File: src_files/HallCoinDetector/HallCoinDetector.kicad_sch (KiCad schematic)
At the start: 30 parts, among them M1 Motor_DC 3V, Q2 BSS214NW, U1 SE555D, U2 TPS61070, U3 49E Hall, U4 LM393

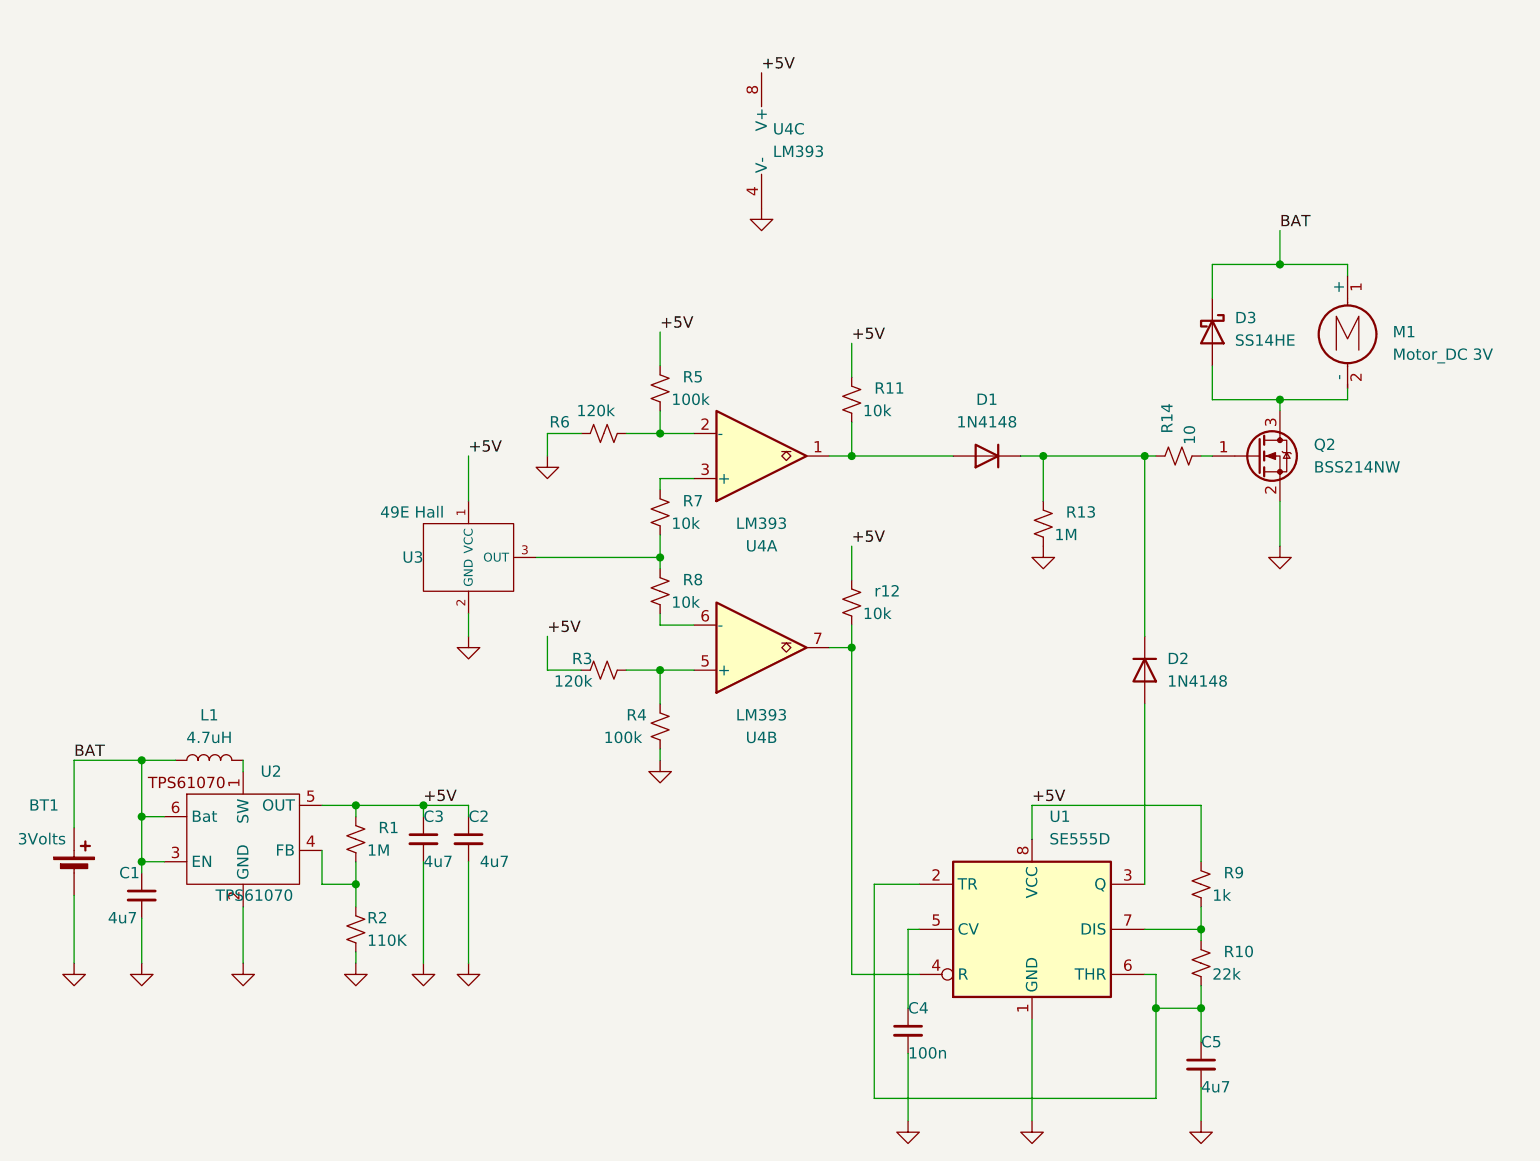
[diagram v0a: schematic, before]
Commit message: diseño de librerias y ubicación de componentes
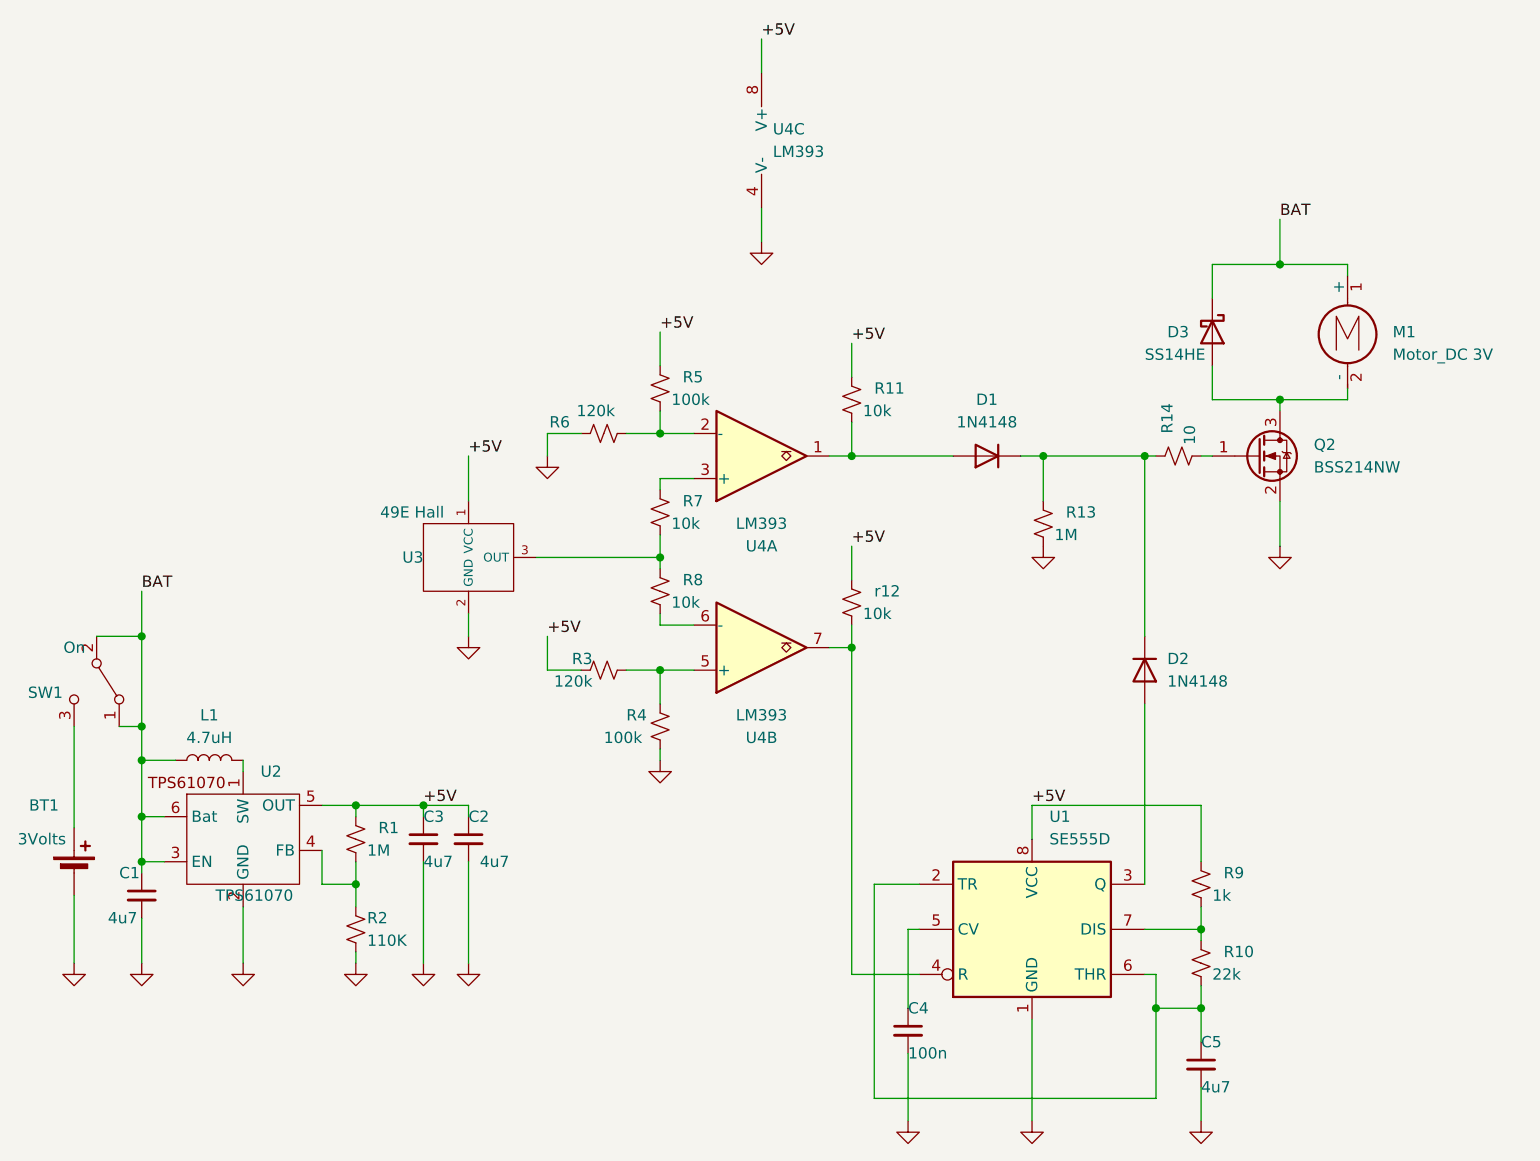
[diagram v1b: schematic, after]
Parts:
- added SW1: On, Button_Switch_SMD:SW_SPDT_PCM12, symbol Switch:SW_SPDT
- BT1: footprint BatteryHolder_Keystone_3002_1x2032 -> Batery Holder:cr1616
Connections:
- net BAT: now also SW1.1 (A), SW1.2 (B); no longer BT1.1 (+)
- new net: BT1.1 (+), SW1.3 (C)

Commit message: delete backups
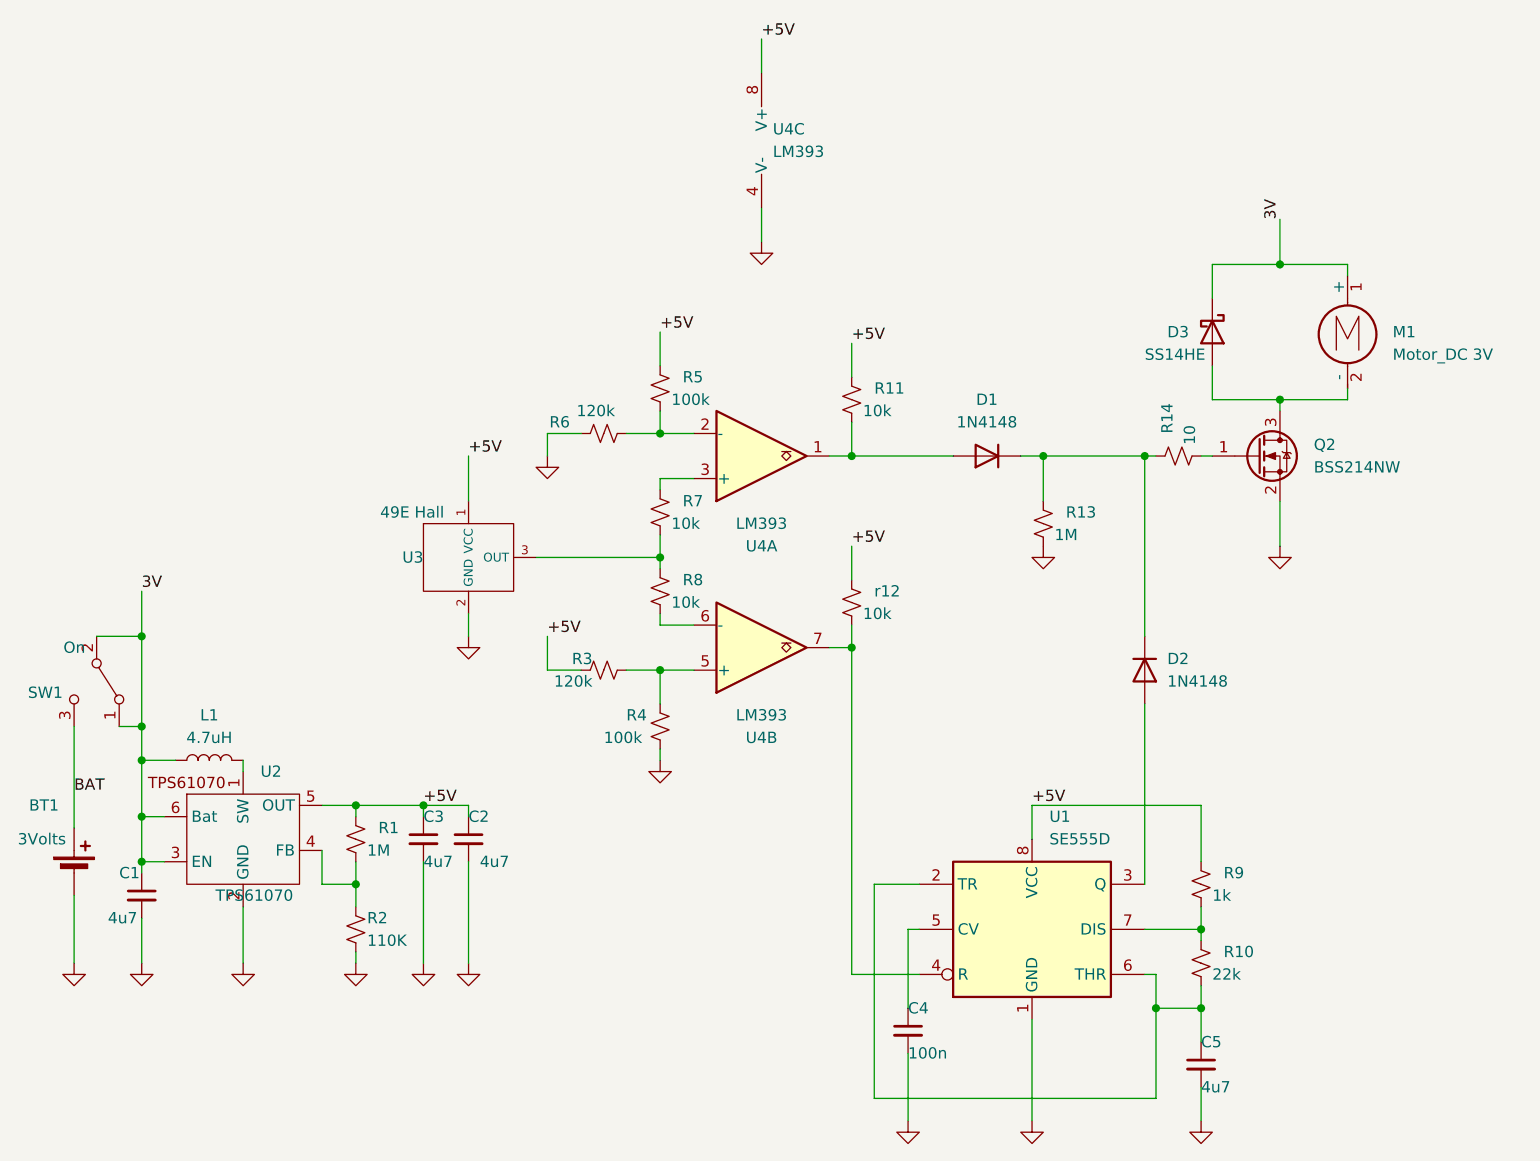
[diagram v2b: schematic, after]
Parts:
- D3: footprint Diode_SMD:D_SOD-323 -> Diode_SMD:D_SOD-123
- U3: footprint Package_TO_SOT_THT:TO-92_Inline_W4.0mm_Horizontal_FlatSideDown -> Package_TO_SOT_SMD:SOT-23-3
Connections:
- net BAT: now also BT1.1 (+), SW1.3 (C); no longer C1.1, D3.1 (K), L1.1, M1.1 (+), SW1.1 (A), SW1.2 (B), U2.3 (EN), U2.6 (Bat)
- new net 3V: C1.1, D3.1 (K), L1.1, M1.1 (+), SW1.1 (A), SW1.2 (B), U2.3 (EN), U2.6 (Bat)
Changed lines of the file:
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@@
     (stroke (width 0) (type default))
   )
-  (label "BAT" (at 154.94 41.91 0) (fields_autoplaced)
-    (effects (font (size 1.27 1.27)) (justify left bottom))
-  )
-  (label "BAT" (at 26.67 83.82 0) (fields_autoplaced)
-    (effects (font (size 1.27 1.27)) (justify left bottom))
-  )
   (label "+5V" (at 127 107.95 0) (fields_autoplaced)
     (effects (font (size 1.27 1.27)) (justify left bottom))
@@
     (effects (font (size 1.27 1.27)) (justify left bottom))
   )
+  (label "3V" (at 26.67 83.82 0) (fields_autoplaced)
+    (effects (font (size 1.27 1.27)) (justify left bottom))
+  )
   (label "+5V" (at 106.68 55.88 0) (fields_autoplaced)
     (effects (font (size 1.27 1.27)) (justify left bottom))
   )
+  (label "BAT" (at 19.05 106.68 0) (fields_autoplaced)
+    (effects (font (size 1.27 1.27)) (justify left bottom))
+  )
   (label "+5V" (at 63.5 68.58 0) (fields_autoplaced)
     (effects (font (size 1.27 1.27)) (justify left bottom))
   )
   (label "+5V" (at 85.09 54.61 0) (fields_autoplaced)
+    (effects (font (size 1.27 1.27)) (justify left bottom))
+  )
+  (label "3V" (at 154.94 41.91 90) (fields_autoplaced)
     (effects (font (size 1.27 1.27)) (justify left bottom))
   )
@@
       (effects (font (size 1.27 1.27)))
     )
-    (property "Footprint" "Package_TO_SOT_THT:TO-92_Inline_W4.0mm_Horizontal_FlatSideDown" (at 62.23 72.39 0)
+    (property "Footprint" "Package_TO_SOT_SMD:SOT-23-3" (at 62.23 72.39 0)
       (effects (font (size 1.27 1.27)) hide)
     )
@@
       (effects (font (size 1.27 1.27)) (justify left))
     )
-    (property "Footprint" "Diode_SMD:D_SOD-323" (at 142.875 54.61 0)
-      (effects (font (size 1.27 1.27)) hide)
-    )
+    (property "Footprint" "Diode_SMD:D_SOD-123" (at 142.875 54.61 0)
+      (effects (font (size 1.27 1.27)) hide)
+    )

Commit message: first_delivery
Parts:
- D1, D2: footprint Diode_THT:D_DO-35_SOD27_P7.62mm_Horizontal -> Diode_SMD:D_0805_2012Metric
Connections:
- net 3V: now also SW1.3 (C); no longer SW1.1 (A), SW1.2 (B)
- net BAT: now also SW1.1 (A), SW1.2 (B); no longer SW1.3 (C)
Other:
- moved on the sheet: SW1
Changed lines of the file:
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@@
     (company "arielrobotti@gmail.com")
   )
+  (junction (at 26.67 102.87) (diameter 0) (color 0 0 0 0)
+  )
   (junction (at 26.67 114.3) (diameter 0) (color 0 0 0 0)
   )
@@
   (junction (at 154.94 62.23) (diameter 0) (color 0 0 0 0)
   )
-  (junction (at 26.67 99.06) (diameter 0) (color 0 0 0 0)
-  )
   (junction (at 85.09 92.71) (diameter 0) (color 0 0 0 0)
   )
@@
   (junction (at 146.05 121.92) (diameter 0) (color 0 0 0 0)
   )
+  (junction (at 19.05 99.06) (diameter 0) (color 0 0 0 0)
+  )
+  (junction (at 26.67 100.33) (diameter 0) (color 0 0 0 0)
+  )
   (junction (at 146.05 130.81) (diameter 0) (color 0 0 0 0)
   )
   (junction (at 26.67 109.22) (diameter 0) (color 0 0 0 0)
   )
-  (junction (at 26.67 88.9) (diameter 0) (color 0 0 0 0)
-  )
   (junction (at 106.68 68.58) (diameter 0) (color 0 0 0 0)
   )
@@
   (junction (at 128.27 68.58) (diameter 0) (color 0 0 0 0)
   )
-  (junction (at 26.67 102.87) (diameter 0) (color 0 0 0 0)
-  )
   (junction (at 106.68 90.17) (diameter 0) (color 0 0 0 0)
   )
@@
     (stroke (width 0) (type default))
   )
+  (wire (pts (xy 19.05 99.06) (xy 19.05 110.49))
+    (stroke (width 0) (type default))
+  )
   (wire (pts (xy 26.67 114.3) (xy 26.67 109.22))
     (stroke (width 0) (type default))
@@
     (stroke (width 0) (type default))
   )
+  (wire (pts (xy 26.67 100.33) (xy 26.67 102.87))
+    (stroke (width 0) (type default))
+  )
   (wire (pts (xy 146.05 130.81) (xy 146.05 134.62))
     (stroke (width 0) (type default))
@@
     (stroke (width 0) (type default))
   )
-  (wire (pts (xy 26.67 88.9) (xy 26.67 99.06))
+  (wire (pts (xy 19.05 88.9) (xy 19.05 99.06))
     (stroke (width 0) (type default))
   )
@@
     (stroke (width 0) (type default))
   )
+  (wire (pts (xy 34.29 100.33) (xy 26.67 100.33))
+    (stroke (width 0) (type default))
+  )
   (wire (pts (xy 85.09 92.71) (xy 88.9 92.71))
     (stroke (width 0) (type default))
   )
-  (wire (pts (xy 24.13 99.06) (xy 26.67 99.06))
+  (wire (pts (xy 21.59 99.06) (xy 19.05 99.06))
     (stroke (width 0) (type default))
   )
@@
     (stroke (width 0) (type default))
   )
-  (wire (pts (xy 19.05 99.06) (xy 19.05 110.49))
-    (stroke (width 0) (type default))
-  )
   (wire (pts (xy 50.8 107.95) (xy 50.8 109.22))
     (stroke (width 0) (type default))
@@
     (stroke (width 0) (type default))
   )
+  (wire (pts (xy 34.29 82.55) (xy 34.29 100.33))
+    (stroke (width 0) (type default))
+  )
   (wire (pts (xy 106.68 90.17) (xy 104.14 90.17))
     (stroke (width 0) (type default))
   )
-  (wire (pts (xy 26.67 99.06) (xy 26.67 102.87))
-    (stroke (width 0) (type default))
-  )
   (wire (pts (xy 46.99 113.03) (xy 46.99 116.84))
     (stroke (width 0) (type default))
@@
     (stroke (width 0) (type default))
   )
+  (wire (pts (xy 26.67 99.06) (xy 26.67 100.33))
+    (stroke (width 0) (type default))
+  )
   (wire (pts (xy 26.67 120.65) (xy 26.67 125.73))
     (stroke (width 0) (type default))
@@
     (stroke (width 0) (type default))
   )
-  (wire (pts (xy 21.59 88.9) (xy 26.67 88.9))
+  (wire (pts (xy 24.13 88.9) (xy 19.05 88.9))
     (stroke (width 0) (type default))
   )
@@
   )
   (wire (pts (xy 109.22 140.97) (xy 140.97 140.97))
-    (stroke (width 0) (type default))
-  )
-  (wire (pts (xy 26.67 83.82) (xy 26.67 88.9))
     (stroke (width 0) (type default))
   )
@@
     (effects (font (size 1.27 1.27)) (justify left bottom))
   )
-  (label "3V" (at 26.67 83.82 0) (fields_autoplaced)
+  (label "3V" (at 34.29 82.55 0) (fields_autoplaced)
     (effects (font (size 1.27 1.27)) (justify left bottom))
   )
@@
     (effects (font (size 1.27 1.27)) (justify left bottom))
   )
-  (symbol (lib_id "Switch:SW_SPDT") (at 21.59 93.98 270) (unit 1)
-    (in_bom yes) (on_board yes) (dnp no)
-    (property "Reference" "SW1" (at 17.78 95.25 90)
+  (symbol (lib_id "Switch:SW_SPDT") (at 24.13 93.98 90) (mirror x) (unit 1)
+    (in_bom yes) (on_board yes) (dnp no)
+    (property "Reference" "SW1" (at 27.94 95.25 90)
       (effects (font (size 1.27 1.27)) (justify right))
     )
-    (property "Value" "On" (at 20.32 90.17 90)
+    (property "Value" "On" (at 25.4 90.17 90)
       (effects (font (size 1.27 1.27)) (justify right))
     )
-    (property "Footprint" "Button_Switch_SMD:SW_SPDT_PCM12" (at 21.59 93.98 0)
-      (effects (font (size 1.27 1.27)) hide)
-    )
-    (property "Datasheet" "~" (at 21.59 93.98 0)
+    (property "Footprint" "Button_Switch_SMD:SW_SPDT_PCM12" (at 24.13 93.98 0)
+      (effects (font (size 1.27 1.27)) hide)
+    )
+    (property "Datasheet" "~" (at 24.13 93.98 0)
       (effects (font (size 1.27 1.27)) hide)
     )
@@
       (effects (font (size 1.27 1.27)))
     )
-    (property "Footprint" "Diode_THT:D_DO-35_SOD27_P7.62mm_Horizontal" (at 121.92 64.135 0)
+    (property "Footprint" "Diode_SMD:D_0805_2012Metric" (at 121.92 64.135 0)
       (effects (font (size 1.27 1.27)) hide)
     )
@@
       (effects (font (size 1.27 1.27)) (justify left))
     )
-    (property "Footprint" "Diode_THT:D_DO-35_SOD27_P7.62mm_Horizontal" (at 135.255 92.71 0)
-      (effects (font (size 1.27 1.27)) hide)
-    )
+    (property "Footprint" "Diode_SMD:D_0805_2012Metric" (at 135.255 92.71 0)
+      (effects (font (size 1.27 1.27)) hide)
+    )

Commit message: panelizado
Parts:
- D1, D2: footprint Diode_SMD:D_0805_2012Metric -> Diode_SMD:D_SOD-123
- D3: footprint Diode_SMD:D_SOD-123 -> Diode_SMD:D_PowerDI-123
- R1, R13: value 1M -> 910k
- R2: value 110K -> 100k
- renumbered r12 to R12
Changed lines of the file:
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@@
       (effects (font (size 1.27 1.27)))
     )
-    (property "Footprint" "Diode_SMD:D_0805_2012Metric" (at 121.92 64.135 0)
+    (property "Footprint" "Diode_SMD:D_SOD-123" (at 121.92 64.135 0)
       (effects (font (size 1.27 1.27)) hide)
     )
@@
       (effects (font (size 1.27 1.27)) (justify left))
     )
-    (property "Value" "1M" (at 129.54 77.47 0)
+    (property "Value" "910k" (at 129.54 77.47 0)
       (effects (font (size 1.27 1.27)) (justify left))
     )
@@
       (effects (font (size 1.27 1.27)) (justify left))
     )
-    (property "Value" "110K" (at 52.07 123.19 0)
+    (property "Value" "100k" (at 52.07 123.19 0)
       (effects (font (size 1.27 1.27)) (justify left))
     )
@@
       (effects (font (size 1.27 1.27)) (justify left))
     )
-    (property "Footprint" "Diode_SMD:D_SOD-123" (at 142.875 54.61 0)
+    (property "Footprint" "Diode_SMD:D_PowerDI-123" (at 142.875 54.61 0)
       (effects (font (size 1.27 1.27)) hide)
     )
@@
   (symbol (lib_id "Device:R_Small_US") (at 106.68 85.09 0) (unit 1)
     (in_bom yes) (on_board yes) (dnp no)
-    (property "Reference" "r12" (at 109.22 83.82 0)
+    (property "Reference" "R12" (at 109.22 83.82 0)
       (effects (font (size 1.27 1.27)) (justify left))
     )
@@
       (project "HallCoinDetector"
         (path "/c2bb8d68-aa11-4de2-9c86-7c4153f3b32d"
-          (reference "r12") (unit 1)
+          (reference "R12") (unit 1)
         )
       )
@@
       (effects (font (size 1.27 1.27)) (justify left))
     )
-    (property "Footprint" "Diode_SMD:D_0805_2012Metric" (at 135.255 92.71 0)
+    (property "Footprint" "Diode_SMD:D_SOD-123" (at 135.255 92.71 0)
       (effects (font (size 1.27 1.27)) hide)
     )
@@
       (effects (font (size 1.27 1.27)) (justify left))
     )
-    (property "Value" "1M" (at 52.07 113.03 0)
-      (effects (font (size 1.27 1.27)) (justify left))
-    )
+    (property "Value" "910k" (at 52.07 113.03 0)
+      (effects (font (size 1.27 1.27)) (justify left))
+    )
